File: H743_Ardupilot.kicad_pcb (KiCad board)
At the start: 6 copper layers, 36.5 x 36.5 mm, 156 parts, among them J1 Analog, J10 Led ext, J11 Buzzer, J12 10067099-200LF, J13 Can1_2, J14 Can1_1, J2 Uart1, J3 Uart4, J4 Uart7, J5 Uart(, J6 Uart6, J7 Uart3, J8 I2C1, J9 I2C_2, Q1 AO3400A, U1 USBLC6-2P6, U10 LSM6DSV16X, U11 ICM-45686, U12 BMP581, U13 DPS368XTSA1, U14 SM08B-SRSS-TB(LF)(SN), U2 STM32H743VIT6, U3 LMR43620R5RPER, U4 LMR604303SRAKRQ1, U5 AP7361C-33FGE-7, U6 AP7361C-33FGE-7, U7 TJA1057GTK/3Z, U8 SM04B-GHS-TB(LF)(SN), U9 BMI088, Y1 8MHz

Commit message: Signed-off-by: oba <Oba@DESKTOP-4RDIH7I>
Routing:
- net /MCU/USB_OTG_P.DP: track 0.00 -> 21.2 mm, vias 0 -> 1
- net /MCU/USB_OTG_P.DM: track 0.00 -> 20.9 mm, vias 0 -> 1
- net /USB_OTG.DN: track 0.00 -> 11.3 mm
- net /USB_OTG.DP: track 0.00 -> 8.04 mm

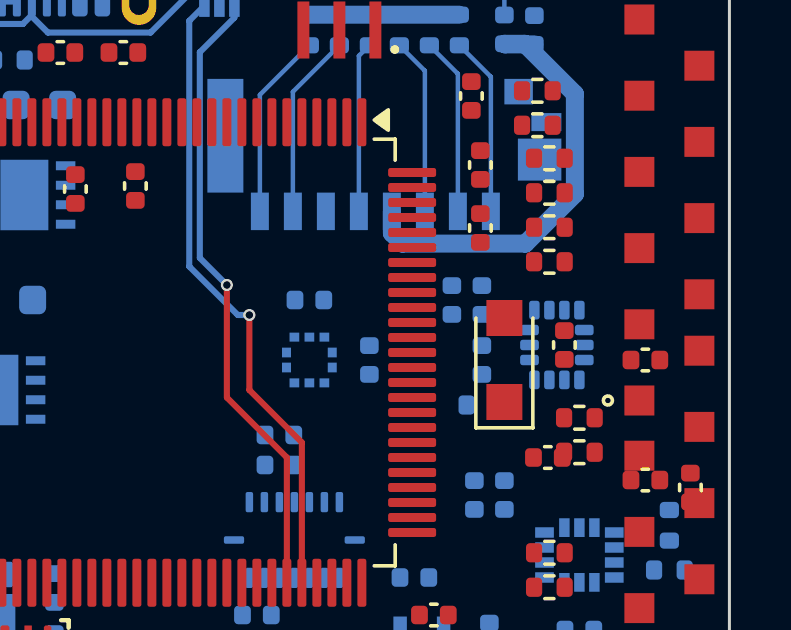
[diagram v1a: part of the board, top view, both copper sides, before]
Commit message: PCB: route SPI4 IMU bus on In3
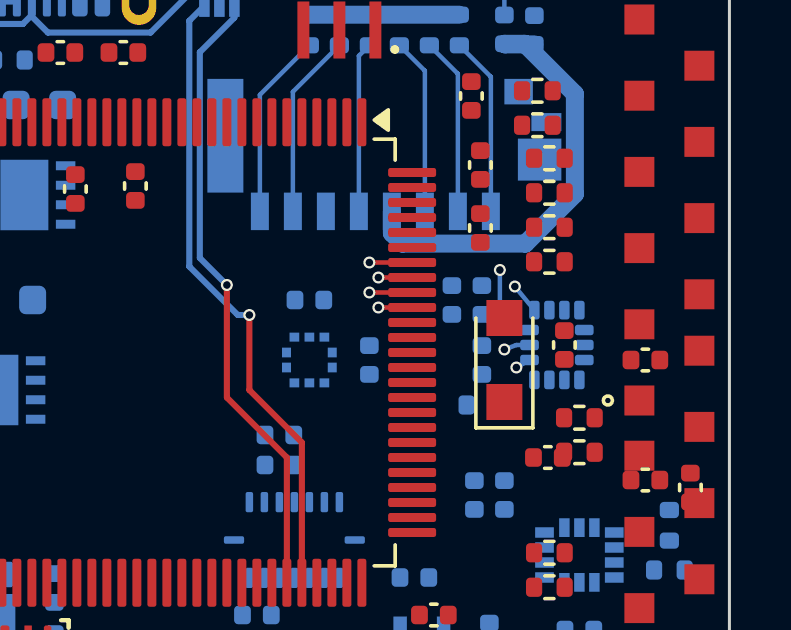
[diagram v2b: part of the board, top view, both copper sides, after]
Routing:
- net /MCU/SPI4.MOSI: track 0.00 -> 8.77 mm, vias 0 -> 2
- net /MCU/SPI4.SCLK: track 0.00 -> 7.17 mm, vias 0 -> 2
- net /MCU/SPI4.MISO: track 0.00 -> 6.71 mm, vias 0 -> 2
- net /MCU/SPI4.CS: track 0.00 -> 6.64 mm, vias 0 -> 2
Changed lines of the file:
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@@
 		(net "/USB_OTG.DN")
+	)
+	(segment
+		(start 100.425 100.75)
+		(end 99 100.75)
+		(width 0.15)
+		(layer "F.Cu")
+		(net "/MCU/SPI4.MOSI")
+	)
+	(via
+		(at 99 100.75)
+		(size 0.4)
+		(drill 0.25)
+		(layers "F.Cu" "B.Cu")
+		(net "/MCU/SPI4.MOSI")
+	)
+	(segment
+		(start 99 100.75)
+		(end 103.35 101)
+		(width 0.15)
+		(layer "In3.Cu")
+		(net "/MCU/SPI4.MOSI")
+	)
+	(via
+		(at 103.35 101)
+		(size 0.4)
+		(drill 0.25)
+		(layers "F.Cu" "B.Cu")
+		(net "/MCU/SPI4.MOSI")
+	)
+	(segment
+		(start 103.35 101)
+		(end 103.35 103)
+		(width 0.15)
+		(layer "B.Cu")
+		(net "/MCU/SPI4.MOSI")
+	)
+	(segment
+		(start 103.35 103)
+		(end 103.9 103)
+		(width 0.15)
+		(layer "B.Cu")
+		(net "/MCU/SPI4.MOSI")
+	)
+	(segment
+		(start 103.9 103)
+		(end 104.3375 103)
+		(width 0.15)
+		(layer "B.Cu")
+		(net "/MCU/SPI4.MOSI")
+	)
+	(segment
+		(start 100.425 101.25)
+		(end 99.3 101.25)
+		(width 0.15)
+		(layer "F.Cu")
+		(net "/MCU/SPI4.MISO")
+	)
+	(via
+		(at 99.3 101.25)
+		(size 0.4)
+		(drill 0.25)
+		(layers "F.Cu" "B.Cu")
+		(net "/MCU/SPI4.MISO")
+	)
+	(segment
+		(start 99.3 101.25)
+		(end 103.85 101.55)
+		(width 0.15)
+		(layer "In3.Cu")
+		(net "/MCU/SPI4.MISO")
+	)
+	(via
+		(at 103.85 101.55)
+		(size 0.4)
+		(drill 0.25)
+		(layers "F.Cu" "B.Cu")
+		(net "/MCU/SPI4.MISO")
+	)
+	(segment
+		(start 103.85 101.55)
+		(end 104.5 102.3375)
+		(width 0.15)
+		(layer "B.Cu")
+		(net "/MCU/SPI4.MISO")
+	)
+	(segment
+		(start 100.425 101.75)
+		(end 99 101.75)
+		(width 0.15)
+		(layer "F.Cu")
+		(net "/MCU/SPI4.SCLK")
+	)
+	(via
+		(at 99 101.75)
+		(size 0.4)
+		(drill 0.25)
+		(layers "F.Cu" "B.Cu")
+		(net "/MCU/SPI4.SCLK")
+	)
+	(segment
+		(start 99 101.75)
+		(end 103.5 103.65)
+		(width 0.15)
+		(layer "In3.Cu")
+		(net "/MCU/SPI4.SCLK")
+	)
+	(via
+		(at 103.5 103.65)
+		(size 0.4)
+		(drill 0.25)
+		(layers "F.Cu" "B.Cu")
+		(net "/MCU/SPI4.SCLK")
+	)
+	(segment
+		(start 103.5 103.65)
+		(end 103.9 103.5)
+		(width 0.15)
+		(layer "B.Cu")
+		(net "/MCU/SPI4.SCLK")
+	)
+	(segment
+		(start 103.9 103.5)
+		(end 104.3375 103.5)
+		(width 0.15)
+		(layer "B.Cu")
+		(net "/MCU/SPI4.SCLK")
+	)
+	(segment
+		(start 100.425 102.25)
+		(end 99.3 102.25)
+		(width 0.15)
+		(layer "F.Cu")
+		(net "/MCU/SPI4.CS")
+	)
+	(via
+		(at 99.3 102.25)
+		(size 0.4)
+		(drill 0.25)
+		(layers "F.Cu" "B.Cu")
+		(net "/MCU/SPI4.CS")
+	)
+	(segment
+		(start 99.3 102.25)
+		(end 103.9 104.25)
+		(width 0.15)
+		(layer "In3.Cu")
+		(net "/MCU/SPI4.CS")
+	)
+	(via
+		(at 103.9 104.25)
+		(size 0.4)
+		(drill 0.25)
+		(layers "F.Cu" "B.Cu")
+		(net "/MCU/SPI4.CS")
+	)
+	(segment
+		(start 103.9 104.25)
+		(end 104.3375 104)
+		(width 0.15)
+		(layer "B.Cu")
+		(net "/MCU/SPI4.CS")
 	)
 	(zone

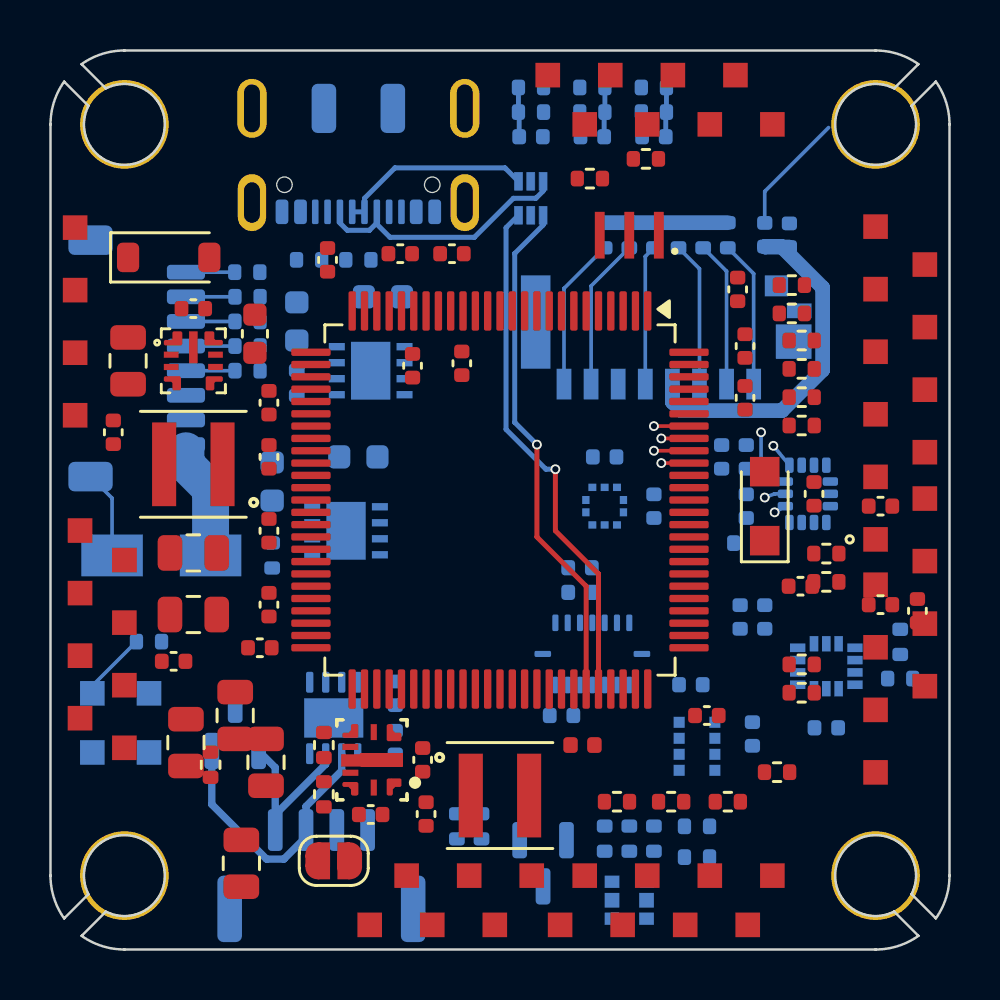
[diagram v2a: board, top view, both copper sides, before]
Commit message: PCB: start routing local power and regulator nets
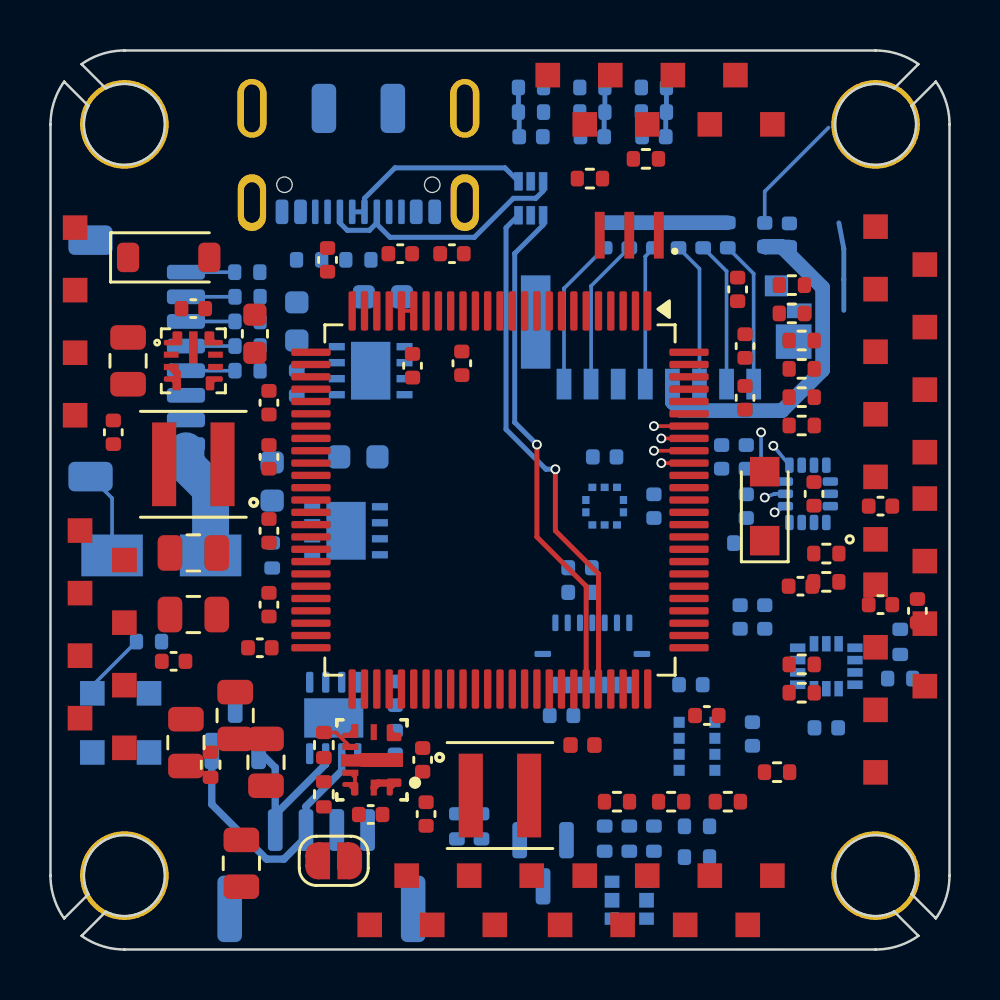
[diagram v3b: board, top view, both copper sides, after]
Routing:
- net +3V3_MCU: track 20.0 -> 23.6 mm
- net VBAT: track 4.75 -> 6.26 mm
- net Net-(U4-FB): track 0.00 -> 1.32 mm
- net Net-(U4-MODE/SYNC): track 0.00 -> 0.87 mm
- net /MCU/VDDA: track 0.00 -> 0.50 mm
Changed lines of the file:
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@@
 		(net "/MCU/SPI4.CS")
+	)
+	(segment
+		(start 89.25 96.075)
+		(end 88.75 96.075)
+		(width 0.15)
+		(layer "F.Cu")
+		(net "/MCU/VDDA")
+	)
+	(segment
+		(start 79.4 98.35)
+		(end 79.6386 98.5886)
+		(width 0.3)
+		(layer "F.Cu")
+		(net "VBAT")
+	)
+	(segment
+		(start 79.6386 98.5886)
+		(end 79.6386 98.9768)
+		(width 0.3)
+		(layer "F.Cu")
+		(net "VBAT")
+	)
+	(segment
+		(start 87.625 115.425)
+		(end 87.8075 115.2425)
+		(width 0.3)
+		(layer "F.Cu")
+		(net "VBAT")
+	)
+	(segment
+		(start 87.8075 115.2425)
+		(end 88.3375 115.2425)
+		(width 0.3)
+		(layer "F.Cu")
+		(net "VBAT")
+	)
+	(segment
+		(start 86.675 114.825)
+		(end 86.8625 115.0125)
+		(width 0.15)
+		(layer "F.Cu")
+		(net "Net-(U4-MODE/SYNC)")
+	)
+	(segment
+		(start 86.8625 115.0125)
+		(end 86.8625 115.6125)
+		(width 0.15)
+		(layer "F.Cu")
+		(net "Net-(U4-MODE/SYNC)")
+	)
+	(segment
+		(start 86.675 113.775)
+		(end 86.09 113.19)
+		(width 0.15)
+		(layer "F.Cu")
+		(net "Net-(U4-FB)")
+	)
+	(segment
+		(start 86.09 113.19)
+		(end 85.6 113.19)
+		(width 0.15)
+		(layer "F.Cu")
+		(net "Net-(U4-FB)")
+	)
+	(segment
+		(start 106.51 92.5)
+		(end 106.71 93.55)
+		(width 0.2)
+		(layer "B.Cu")
+		(net "+3V3_MCU")
+	)
+	(segment
+		(start 106.71 93.55)
+		(end 106.71 94.8)
+		(width 0.2)
+		(layer "B.Cu")
+		(net "+3V3_MCU")
+	)
+	(segment
+		(start 106.71 94.8)
+		(end 106.71 96.05)
+		(width 0.2)
+		(layer "B.Cu")
+		(net "+3V3_MCU")
 	)
 	(zone

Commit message: PCB: remove unsafe first-pass routes after KiCad 10 DRC
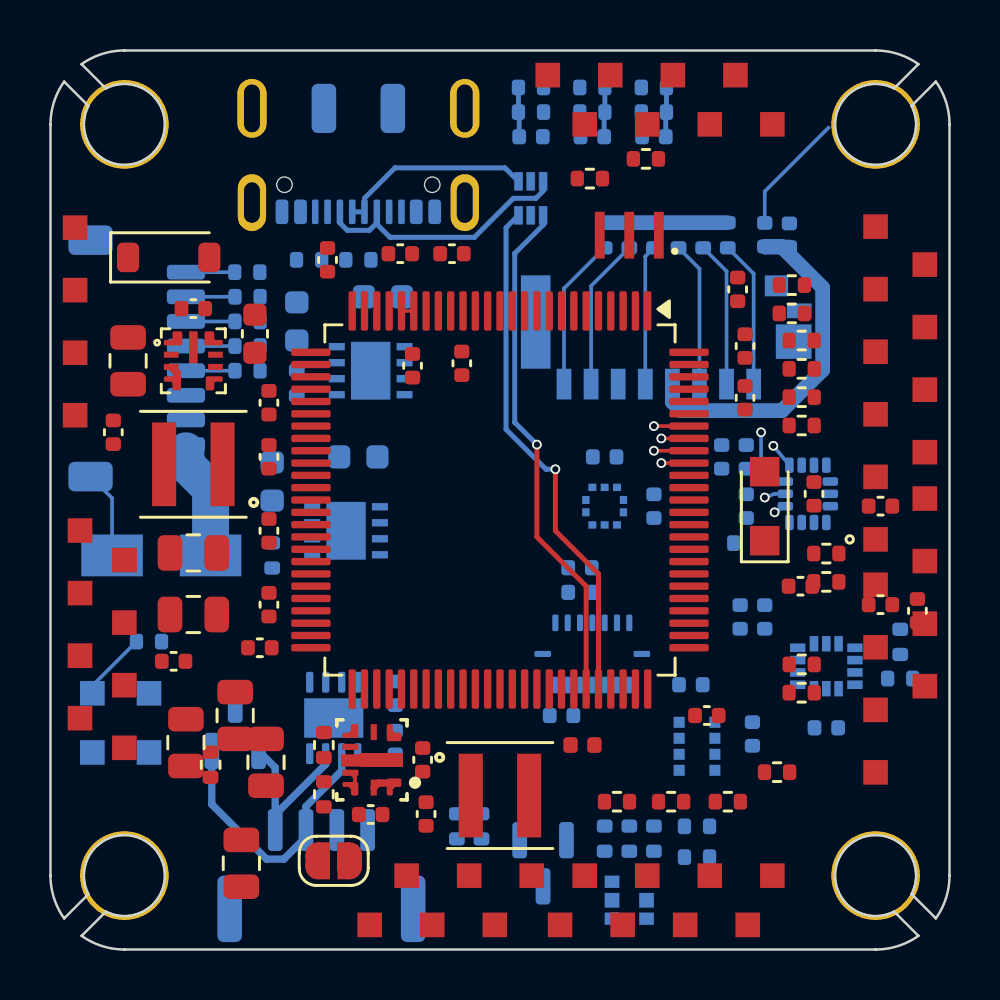
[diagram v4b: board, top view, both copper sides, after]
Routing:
- net +3V3_MCU: track 23.6 -> 20.0 mm
- net Net-(U4-FB): track 1.32 -> 0.00 mm
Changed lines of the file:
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@@
 		(net "Net-(U4-MODE/SYNC)")
-	)
-	(segment
-		(start 86.675 113.775)
-		(end 86.09 113.19)
-		(width 0.15)
-		(layer "F.Cu")
-		(net "Net-(U4-FB)")
-	)
-	(segment
-		(start 86.09 113.19)
-		(end 85.6 113.19)
-		(width 0.15)
-		(layer "F.Cu")
-		(net "Net-(U4-FB)")
-	)
-	(segment
-		(start 106.51 92.5)
-		(end 106.71 93.55)
-		(width 0.2)
-		(layer "B.Cu")
-		(net "+3V3_MCU")
-	)
-	(segment
-		(start 106.71 93.55)
-		(end 106.71 94.8)
-		(width 0.2)
-		(layer "B.Cu")
-		(net "+3V3_MCU")
-	)
-	(segment
-		(start 106.71 94.8)
-		(end 106.71 96.05)
-		(width 0.2)
-		(layer "B.Cu")
-		(net "+3V3_MCU")
 	)
 	(zone

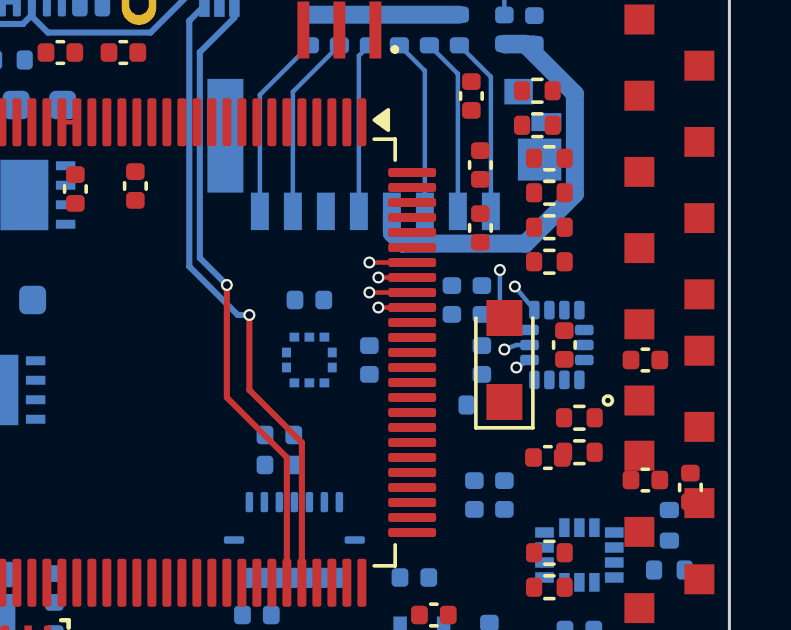
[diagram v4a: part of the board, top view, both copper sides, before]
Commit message: PCB: remove invalid SPI4 prototype routing
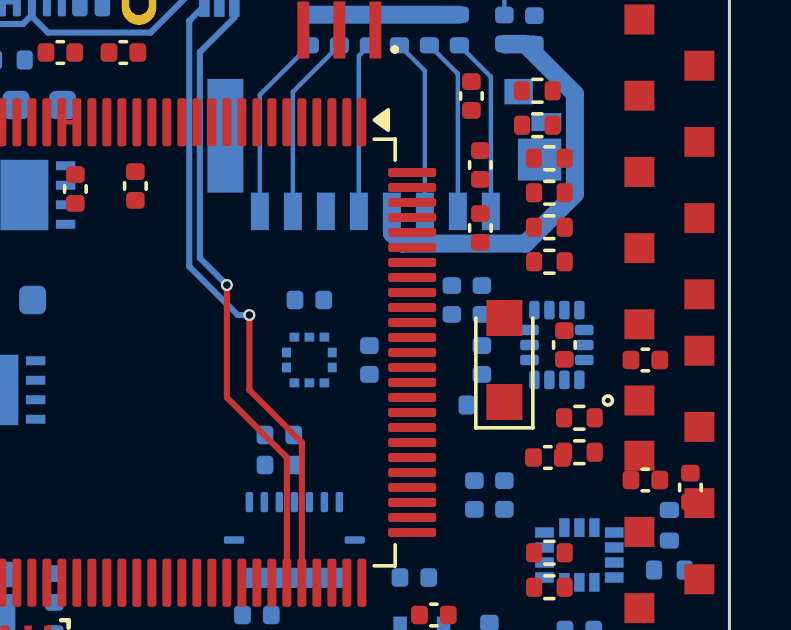
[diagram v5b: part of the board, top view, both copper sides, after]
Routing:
- net /MCU/SPI4.MOSI: track 8.77 -> 0.00 mm, vias 2 -> 0
- net /MCU/SPI4.SCLK: track 7.17 -> 0.00 mm, vias 2 -> 0
- net /MCU/SPI4.MISO: track 6.71 -> 0.00 mm, vias 2 -> 0
- net /MCU/SPI4.CS: track 6.64 -> 0.00 mm, vias 2 -> 0
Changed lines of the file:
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@@
-	)
-	(segment
-		(start 100.425 100.75)
-		(end 99 100.75)
-		(width 0.15)
-		(layer "F.Cu")
-		(net "/MCU/SPI4.MOSI")
-	)
-	(via
-		(at 99 100.75)
-		(size 0.4)
-		(drill 0.25)
-		(layers "F.Cu" "B.Cu")
-		(net "/MCU/SPI4.MOSI")
-	)
-	(segment
-		(start 99 100.75)
-		(end 103.35 101)
-		(width 0.15)
-		(layer "In3.Cu")
-		(net "/MCU/SPI4.MOSI")
-	)
-	(via
-		(at 103.35 101)
-		(size 0.4)
-		(drill 0.25)
-		(layers "F.Cu" "B.Cu")
-		(net "/MCU/SPI4.MOSI")
-	)
-	(segment
-		(start 103.35 101)
-		(end 103.35 103)
-		(width 0.15)
-		(layer "B.Cu")
-		(net "/MCU/SPI4.MOSI")
-	)
-	(segment
-		(start 103.35 103)
-		(end 103.9 103)
-		(width 0.15)
-		(layer "B.Cu")
-		(net "/MCU/SPI4.MOSI")
-	)
-	(segment
-		(start 103.9 103)
-		(end 104.3375 103)
-		(width 0.15)
-		(layer "B.Cu")
-		(net "/MCU/SPI4.MOSI")
-	)
-	(segment
-		(start 100.425 101.25)
-		(end 99.3 101.25)
-		(width 0.15)
-		(layer "F.Cu")
-		(net "/MCU/SPI4.MISO")
-	)
-	(via
-		(at 99.3 101.25)
-		(size 0.4)
-		(drill 0.25)
-		(layers "F.Cu" "B.Cu")
-		(net "/MCU/SPI4.MISO")
-	)
-	(segment
-		(start 99.3 101.25)
-		(end 103.85 101.55)
-		(width 0.15)
-		(layer "In3.Cu")
-		(net "/MCU/SPI4.MISO")
-	)
-	(via
-		(at 103.85 101.55)
-		(size 0.4)
-		(drill 0.25)
-		(layers "F.Cu" "B.Cu")
-		(net "/MCU/SPI4.MISO")
-	)
-	(segment
-		(start 103.85 101.55)
-		(end 104.5 102.3375)
-		(width 0.15)
-		(layer "B.Cu")
-		(net "/MCU/SPI4.MISO")
-	)
-	(segment
-		(start 100.425 101.75)
-		(end 99 101.75)
-		(width 0.15)
-		(layer "F.Cu")
-		(net "/MCU/SPI4.SCLK")
-	)
-	(via
-		(at 99 101.75)
-		(size 0.4)
-		(drill 0.25)
-		(layers "F.Cu" "B.Cu")
-		(net "/MCU/SPI4.SCLK")
-	)
-	(segment
-		(start 99 101.75)
-		(end 103.5 103.65)
-		(width 0.15)
-		(layer "In3.Cu")
-		(net "/MCU/SPI4.SCLK")
-	)
-	(via
-		(at 103.5 103.65)
-		(size 0.4)
-		(drill 0.25)
-		(layers "F.Cu" "B.Cu")
-		(net "/MCU/SPI4.SCLK")
-	)
-	(segment
-		(start 103.5 103.65)
-		(end 103.9 103.5)
-		(width 0.15)
-		(layer "B.Cu")
-		(net "/MCU/SPI4.SCLK")
-	)
-	(segment
-		(start 103.9 103.5)
-		(end 104.3375 103.5)
-		(width 0.15)
-		(layer "B.Cu")
-		(net "/MCU/SPI4.SCLK")
-	)
-	(segment
-		(start 100.425 102.25)
-		(end 99.3 102.25)
-		(width 0.15)
-		(layer "F.Cu")
-		(net "/MCU/SPI4.CS")
-	)
-	(via
-		(at 99.3 102.25)
-		(size 0.4)
-		(drill 0.25)
-		(layers "F.Cu" "B.Cu")
-		(net "/MCU/SPI4.CS")
-	)
-	(segment
-		(start 99.3 102.25)
-		(end 103.9 104.25)
-		(width 0.15)
-		(layer "In3.Cu")
-		(net "/MCU/SPI4.CS")
-	)
-	(via
-		(at 103.9 104.25)
-		(size 0.4)
-		(drill 0.25)
-		(layers "F.Cu" "B.Cu")
-		(net "/MCU/SPI4.CS")
-	)
-	(segment
-		(start 103.9 104.25)
-		(end 104.3375 104)
-		(width 0.15)
-		(layer "B.Cu")
-		(net "/MCU/SPI4.CS")
 	)
 	(segment

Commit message: update powersupplie
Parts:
- moved R6 1.12 mm to (81.5, 115.5)
- moved C26 0.78 mm to (79.5, 113.0)
- moved C18 0.76 mm to (84.0, 114.5)
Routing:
- net Net-(U4-MODE/SYNC): track 0.00 -> 0.87 mm
- net Net-(U4-MODE/SYNC): track 0.87 -> 0.00 mm
- net VDDA: track 0.00 -> 0.50 mm
- net /MCU/VDDA: track 0.50 -> 0.00 mm
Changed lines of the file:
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@@
 	(footprint "Capacitor_SMD:C_0805_2012Metric"
 		(layer "F.Cu")
-		(at 83.25 114.4 90)
+		(at 84 114.5 90)
 		(descr "Capacitor SMD 0805 (2012 Metric), square (rectangular) end terminal, IPC-7351 nominal, (Body size source: IPC-SM-782 page 76, https://www.pcb-3d.com/wordpress/wp-content/uploads/ipc-sm-782a_amendment_1_and_2.pdf, https://docs.google.com/spreadsheets/d/1BsfQQcO9C6DZCsRaXUlFlo91Tg2WpOkGARC1WS5S8t0/edit?usp=sharing)")
 		(tags "capacitor")
@@
 	(footprint "Capacitor_SMD:C_0805_2012Metric"
 		(layer "F.Cu")
-		(at 80 113.6 90)
+		(at 79.5 113 90)
 		(descr "Capacitor SMD 0805 (2012 Metric), square (rectangular) end terminal, IPC-7351 nominal, (Body size source: IPC-SM-782 page 76, https://www.pcb-3d.com/wordpress/wp-content/uploads/ipc-sm-782a_amendment_1_and_2.pdf, https://docs.google.com/spreadsheets/d/1BsfQQcO9C6DZCsRaXUlFlo91Tg2WpOkGARC1WS5S8t0/edit?usp=sharing)")
 		(tags "capacitor")
@@
 	(footprint "Resistor_SMD:R_0402_1005Metric"
 		(layer "F.Cu")
-		(at 81 114.5 -90)
+		(at 81.5 115.5 -90)
 		(descr "Resistor SMD 0402 (1005 Metric), square (rectangular) end terminal, IPC-7351 nominal, (Body size source: IPC-SM-782 page 72, https://www.pcb-3d.com/wordpress/wp-content/uploads/ipc-sm-782a_amendment_1_and_2.pdf)")
 		(tags "resistor")
@@
 	)
 	(segment
+		(start 87.8075 115.2425)
+		(end 88.3375 115.2425)
+		(width 0.3)
+		(layer "F.Cu")
+		(net "VBAT")
+	)
+	(segment
+		(start 79.4 98.35)
+		(end 79.6386 98.5886)
+		(width 0.3)
+		(layer "F.Cu")
+		(net "VBAT")
+	)
+	(segment
+		(start 79.6386 98.5886)
+		(end 79.6386 98.9768)
+		(width 0.3)
+		(layer "F.Cu")
+		(net "VBAT")
+	)
+	(segment
+		(start 87.625 115.425)
+		(end 87.8075 115.2425)
+		(width 0.3)
+		(layer "F.Cu")
+		(net "VBAT")
+	)
+	(segment
 		(start 81 106)
 		(end 81 103.3)
@@
 	)
 	(segment
+		(start 89.25 96.075)
+		(end 88.75 96.075)
+		(width 0.15)
+		(layer "F.Cu")
+		(net "VDDA")
+	)
+	(segment
 		(start 93.5 88)
 		(end 93.5 87)
@@
 	)
 	(segment
+		(start 86.8625 115.0125)
+		(end 86.8625 115.6125)
+		(width 0.15)
+		(layer "F.Cu")
+		(net "Net-(U4-MODE{slash}SYNC)")
+	)
+	(segment
+		(start 86.675 114.825)
+		(end 86.8625 115.0125)
+		(width 0.15)
+		(layer "F.Cu")
+		(net "Net-(U4-MODE{slash}SYNC)")
+	)
+	(segment
 		(start 80 97.5)
 		(end 81.99 97.5)
@@
 		(net "/USB_OTG.DN")
 	)
-	(segment
-		(start 89.25 96.075)
-		(end 88.75 96.075)
-		(width 0.15)
-		(layer "F.Cu")
-		(net "/MCU/VDDA")
-	)
-	(segment
-		(start 79.4 98.35)
-		(end 79.6386 98.5886)
-		(width 0.3)
-		(layer "F.Cu")
-		(net "VBAT")
-	)
-	(segment
-		(start 79.6386 98.5886)
-		(end 79.6386 98.9768)
-		(width 0.3)
-		(layer "F.Cu")
-		(net "VBAT")
-	)
-	(segment
-		(start 87.625 115.425)
-		(end 87.8075 115.2425)
-		(width 0.3)
-		(layer "F.Cu")
-		(net "VBAT")
-	)
-	(segment
-		(start 87.8075 115.2425)
-		(end 88.3375 115.2425)
-		(width 0.3)
-		(layer "F.Cu")
-		(net "VBAT")
-	)
-	(segment
-		(start 86.675 114.825)
-		(end 86.8625 115.0125)
-		(width 0.15)
-		(layer "F.Cu")
-		(net "Net-(U4-MODE/SYNC)")
-	)
-	(segment
-		(start 86.8625 115.0125)
-		(end 86.8625 115.6125)
-		(width 0.15)
-		(layer "F.Cu")
-		(net "Net-(U4-MODE/SYNC)")
-	)
 	(zone
